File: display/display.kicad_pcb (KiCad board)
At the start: 4 copper layers, 162 x 65.4 mm, 19 parts, among them J1 DIN41612_03x32_ABC

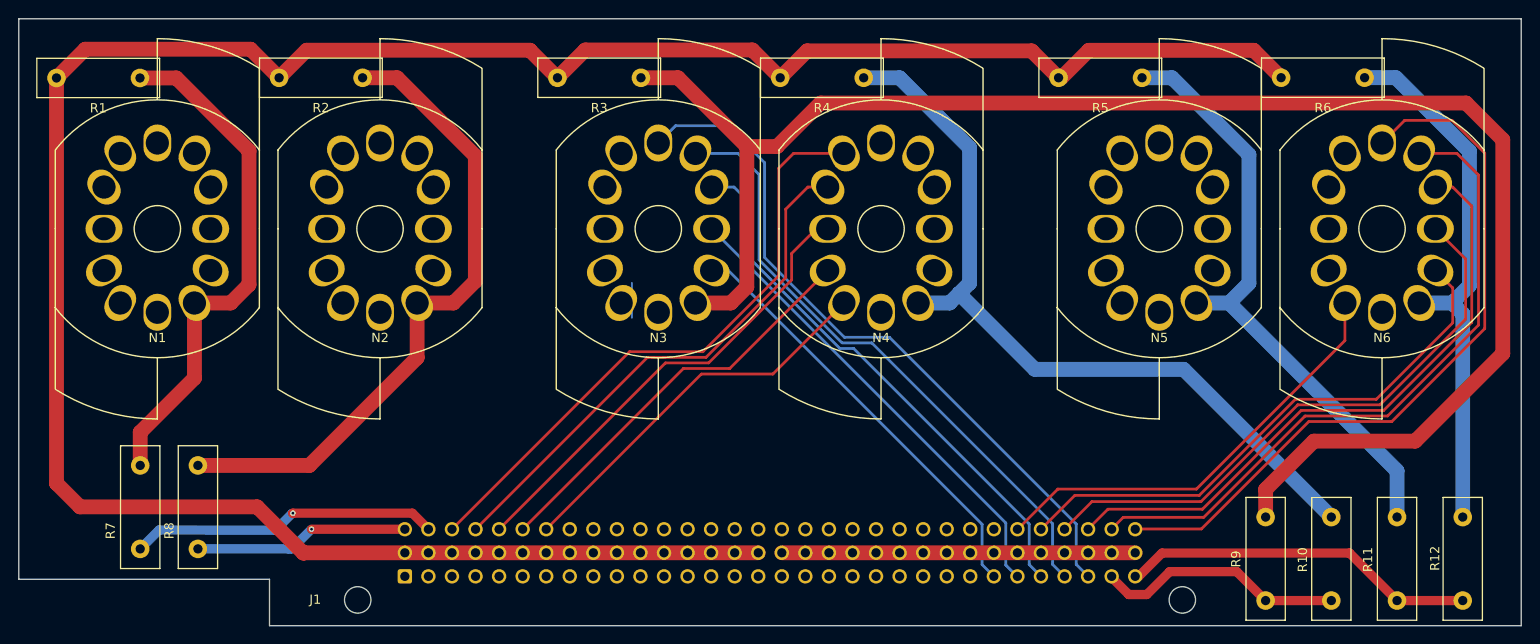
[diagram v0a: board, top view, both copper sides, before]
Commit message: Display board is completely routed
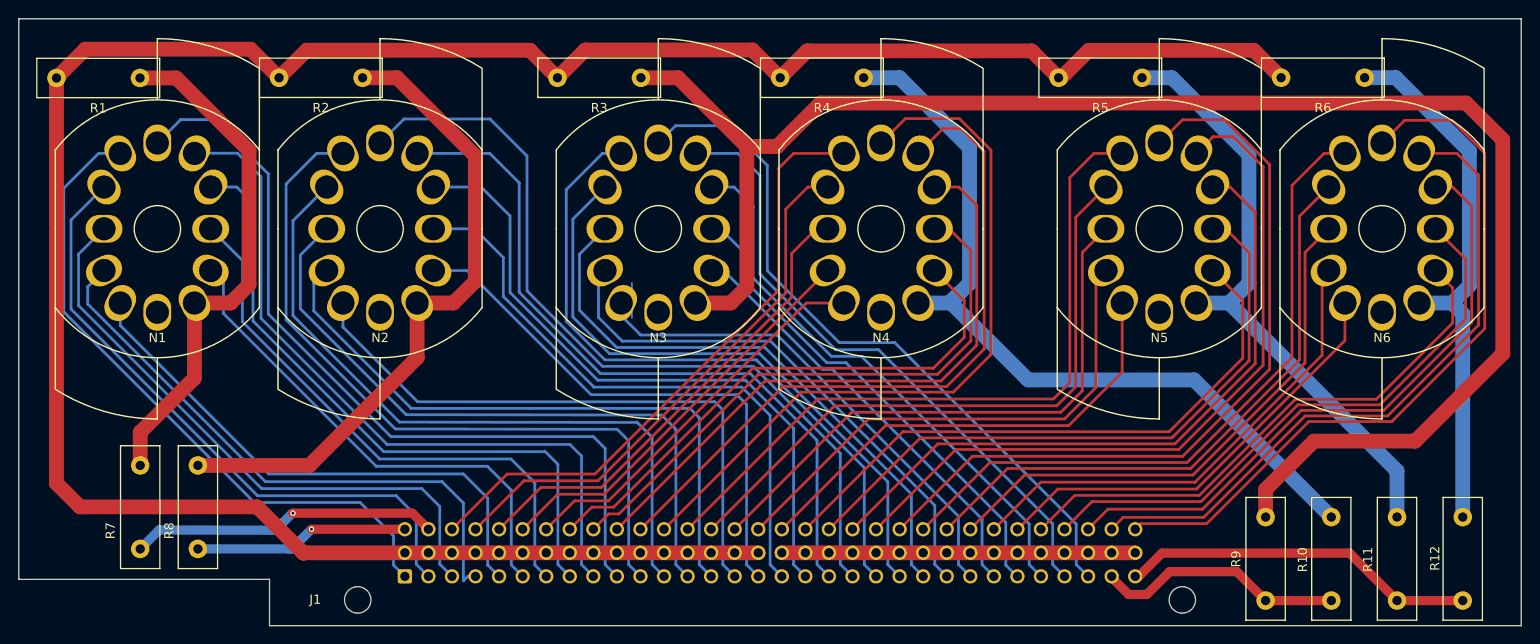
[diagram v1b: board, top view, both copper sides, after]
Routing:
- net /T2-6: track 0.00 -> 87.9 mm
- net /T1-6: track 0.00 -> 87.2 mm
- net /T5-6: track 0.00 -> 84.0 mm
- net /T5-7: track 0.00 -> 79.7 mm
- net /T2-5: track 0.00 -> 79.5 mm
- net /T4-6: track 0.00 -> 79.4 mm
- net /T2-7: track 0.00 -> 78.0 mm
- net /T1-7: track 0.00 -> 77.7 mm
- net /T5-5: track 0.00 -> 76.6 mm
- net /T4-7: track 0.00 -> 75.6 mm
- net /T2-4: track 0.00 -> 74.9 mm
- net /T6-5: track 0.00 -> 73.1 mm
- net /T5-8: track 0.00 -> 72.9 mm
- net /T3-5: track 0.00 -> 72.6 mm
- net /T2-3: track 0.00 -> 71.9 mm
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
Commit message: Minor corrections and evaluate DRC warnings
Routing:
- net GND: track 38.1 -> 121.2 mm
- net /T3-1: track 57.4 -> 54.1 mm
- net /T1-2: track 63.6 -> 62.4 mm
- net /T1-7: track 77.7 -> 77.0 mm
- net /T1-1: track 58.7 -> 58.0 mm
- added copper zone on In1.Cu, net GND
- added copper zone on In2.Cu, net GND
